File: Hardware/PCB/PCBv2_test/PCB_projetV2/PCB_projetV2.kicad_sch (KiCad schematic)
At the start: 43 parts, among them J1 Conn_01x02, J10 Conn_02x03_Odd_Even, J11 R-78B5.0-2.0, J12 Conn_01x04, J13 Conn_01x02, J14 Conn_01x02, J2 Conn_01x04, J3 BU33SD5WG-TR, J4 Conn_01x06, J5 Conn_01x03, J6 Conn_01x03, J7 Conn_ST_STDC14, J8 Conn_01x06, J9 Conn_01x06, U1 STM32L552CCTx

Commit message: finalisation PCB v2
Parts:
- J5, J6: footprint Connector_JST:JST_XH_B3B-XH-A_1x03_P2.50mm_Vertical -> Connector_JST:JST_PH_B3B-PH-K_1x03_P2.00mm_Vertical
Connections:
- net AIN1: now also U1.33 (PA12); no longer U1.32 (PA11)
- net AIN2: now also U1.32 (PA11); no longer U1.33 (PA12)
- net +7.5V renamed +12V

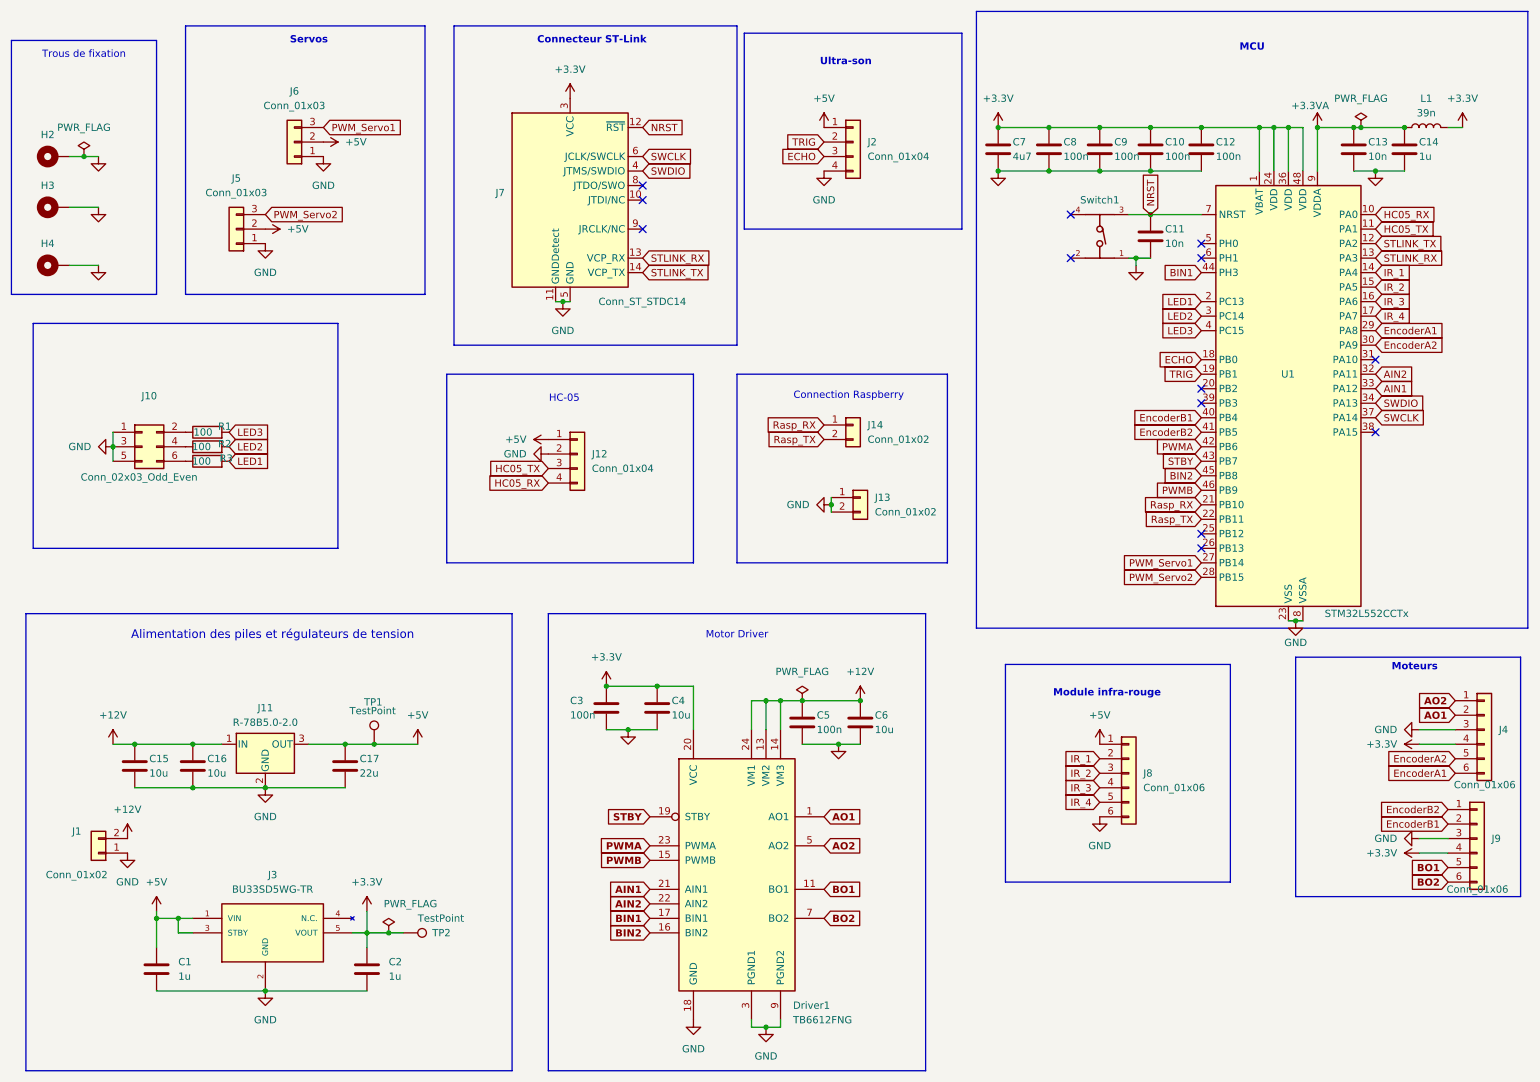
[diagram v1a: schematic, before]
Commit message: ajout des condensateurs pour les modules
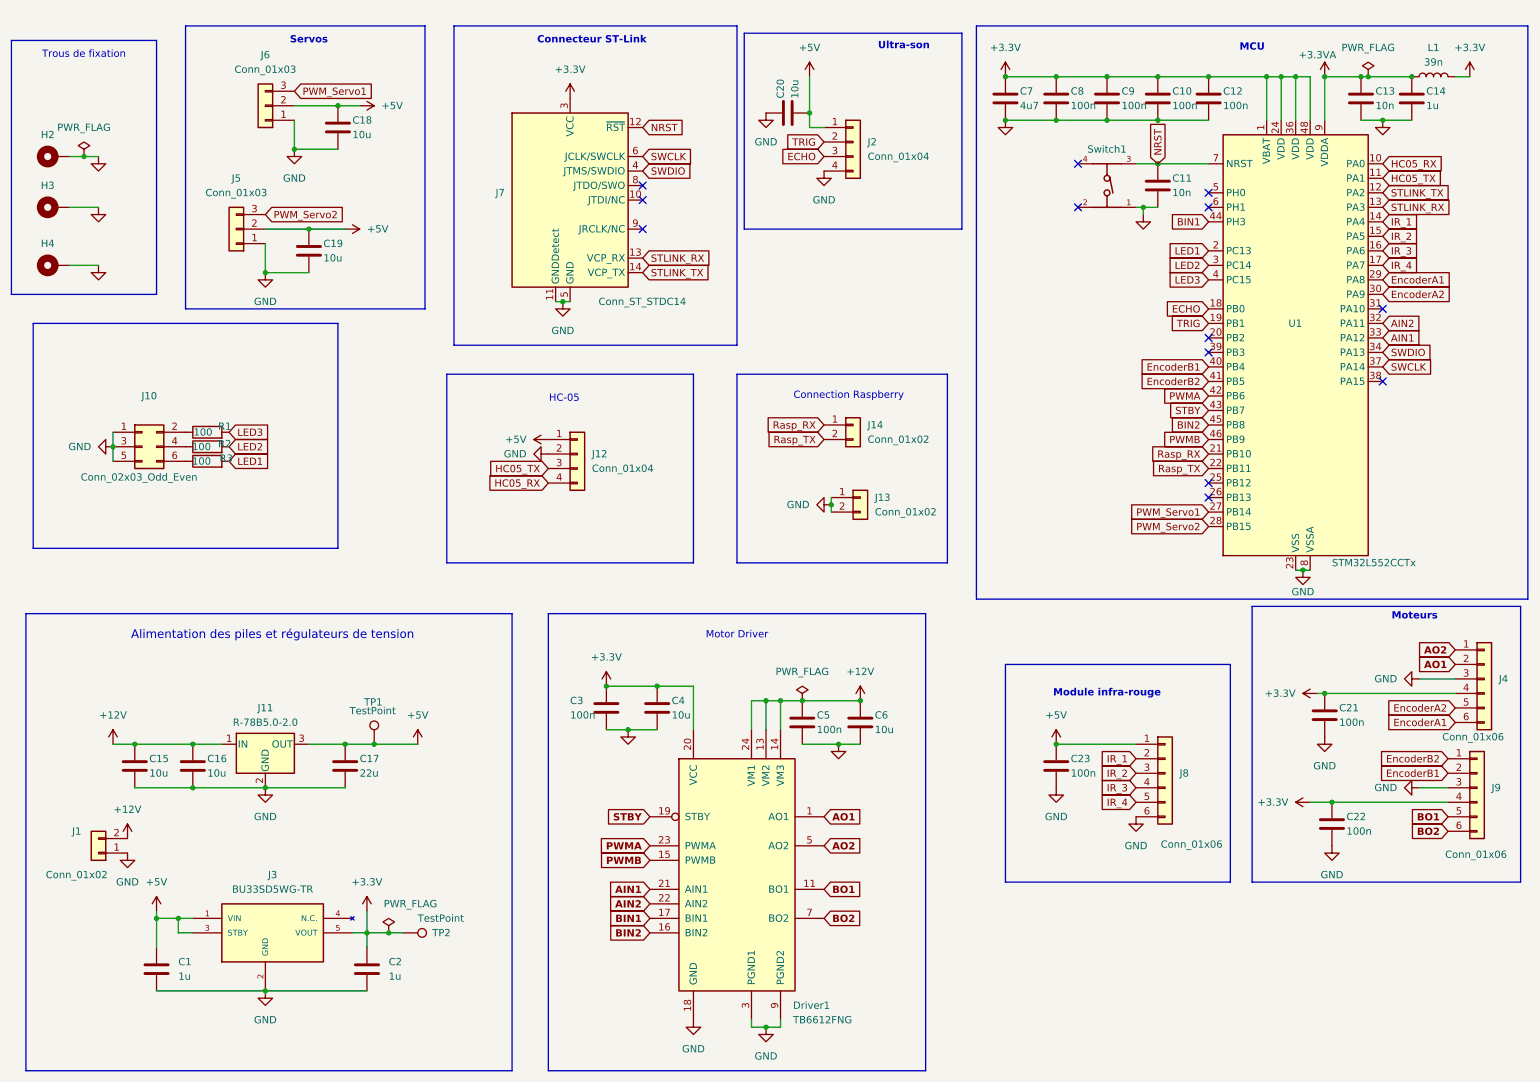
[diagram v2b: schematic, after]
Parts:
- added C18, C19, C20: 10u, Capacitor_SMD:C_0603_1608Metric, symbol Device:C
- added C21, C22, C23: 100n, Capacitor_SMD:C_0402_1005Metric, symbol Device:C
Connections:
- net +3.3V: now also C21.1, C22.1
- net +5V: now also C18.1, C19.1, C20.2, C23.1
- net GND: now also C18.2, C19.2, C20.1, C21.2, C22.2, C23.2
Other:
- moved on the sheet: C10, C11, C12, C13, C14, C7, C8, C9, J4, J6, J8, J9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
